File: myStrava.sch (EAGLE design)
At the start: 43 parts, among them Y1 16MHz

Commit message: Avant autoroutage
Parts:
- removed MAX17043: MAX1704X, SparkFun-PowerIC:MAX1704X
- removed R13, R14: 10k, SparkFun-Resistors:RESISTOR1206
- added JTAG1: 2X5_0.05"_CORTEX_DEBUGTH_NOKEY_UNSHROUDED, con-cortex:2X5_0.05"_CORTEX_DEBUGTH_NOKEY_UNSHROUDED
- added U$1: STC3100, STC3100:STC3100
- C1: value 1uF -> 220nF
- C4, C5: value 4.7uF -> 10uF
- R3: value 1k -> 200k/0.1%
- R4: value 180 -> 0.02
- R7: value 4.7k -> 1kOhms
- R8, R9: device SparkFun-Resistors:RESISTOR1206 -> SparkFun-Resistors:RESISTOR0805-RES
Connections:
- removed net N$29: MK20DN512.PTB18, NAV.2
- removed net N$30: MK20DN512.PTB19, NAV.T
- removed net N$31: MK20DN512.PTB0, NAV.1
- removed net N$33: R14.1, SST25.WP
- removed net N$34: R13.2, SST25.HOLD
- new net N$10: N550.NONE1, NAV.2
- new net N$11: N550.SUSPEND, NAV.T
- new net N$12: N550.SLEEP, NAV.1
- new net N$13: N550.NONE2, NAV.C
- new net N$15: MK20DN512.PTB23, SST25.WP
- new net N$24: MK20DN512.PTB22, SST25.HOLD
- new net N$5: C1.1, R7.1, U$1.VIN
- new net N$6: BATT.2, R4.2, U$1.CG
- new net N$9: N550.PORTSEL, SPK.2
- new net VCC: JTAG1.VCC
- net GND: now also C1.2, JTAG1.GND, JTAG1.GND-DETECT, R3.2, R4.1, U$1.GND; no longer BATT.2, C1.1, MAX17043.CTG, MAX17043.GND@4, MAX17043.GND@EP, NAV.C, R7.2, SPK.2
- net MK_SCL: now also U$1.SCL; no longer MAX17043.SCL
- net MK_SDA: now also U$1.SDA; no longer MAX17043.SDA
- net N$3: now also JTAG1.SWDIO/TMS, N550.RST; no longer MK20DN512.PTB1, SPK.1
- net N$4: now also R3.1, U$1.ROSC; no longer C1.2, MAX17043.CELL, R3.2
- net N$7: now also JTAG1.SWDCLK/TCK, N550.NONE3; no longer MAX17043.VDD, R4.2
- net N$8: now also N550.SCLK, SPK.1; no longer MAX17043.QST, R7.1
- net VCC-ISO: now also R7.2, U$1.VCC; no longer R3.1, R4.1
- net VDD: no longer R13.1, R14.2
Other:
- moved on the sheet: C1, NAV, R3, R4, R7, SPK

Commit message: Version avec MK64
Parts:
- added D2: OSRAM, SparkFun-LED:LED-RED1206
- added D3: Diode, adafruit:DIODE_SOD-123FL
- added PTE2, PTE3, RX2, SCL, SDA: MDMK2020T4R7MM, Exposed_pad:MDMK2020T4R7MM
- added R13: 50ohms, SparkFun-Resistors:RESISTOR1206
- added R14: 10K, SparkFun-Resistors:RESISTOR1206
- added TX2: TX2, Exposed_pad:MDMK2020T4R7MM
- renumbered LDO33 to LDO0, U$1 to STC3100
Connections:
- removed net VDD: BMP180.VDD, BMP180.VDDIO, C2.P$1, C3.P$1, C6.P$1, C7.P$1, C8.P$1, C9.P$1, JTAG.VCC, LDO0.OUT, MK20DN512.VBAT, MK20DN512.VDD, MK20DN512.VDD1, MK20DN512.VDD2, MK20DN512.VDD3, MK20DN512.VDD4, MK20DN512.VDD5, MK20DN512.VDDA, MK20DN512.VOUT33, MK20DN512.VREFH, MT3339.VCC, N550.VCC, R12.2, R5.1, R6.1, SD.VCC, SHARP.VDD, SHARP.VDDA, SST25.VDD
- new net END_CHARGE: MCP73831.STAT, MK20DN512.PTB0, R2.2
- new net MK_RX2: MK20DN512.PTE1, RX2.1
- new net MK_TX2: MK20DN512.PTE0, TX2.1
- new net MK_USB_DETECT: MK20DN512.PTE5, R14.1
- new net N$28: MK20DN512.PTE2, PTE2.1
- new net N$30: MK20DN512.PTE3, PTE3.1
- new net N$31: MK20DN512.PTB1, R13.1
- new net USB_V+: C4.1, D1.A, D3.A, MCP73831.VDD, R14.2, USB.VBUS
- net MK_SCL: now also SCL.1
- net MK_SDA: now also SDA.1
- net N$17: now also D2.C, R13.2; no longer MCP73831.STAT, R2.2
- net N$18: now also MK20DN512.PTD1, N550.BR1; no longer C4.1, D1.A, MCP73831.VDD, USB.VBUS
- net N$21: now also MK20DN512.PTD0, N550.SPD_SEL; no longer MK20DN512.PTD4, N550.BR1
- net VCC: now also BMP180.VDD, BMP180.VDDIO, C2.P$1, C3.P$1, C6.P$1, C7.P$1, C8.P$1, C9.P$1, D2.A, JTAG.VCC, LDO0.OUT, MK20DN512.VBAT, MK20DN512.VDD, MK20DN512.VDD1, MK20DN512.VDD2, MK20DN512.VDD3, MK20DN512.VDD4, MK20DN512.VDD5, MK20DN512.VDDA, MK20DN512.VOUT33, MK20DN512.VREFH, MT3339.VCC, N550.VCC, R12.2, R5.1, R6.1, SD.VCC, SHARP.VDD, SHARP.VDDA, SST25.VDD
- net VCC-ISO: now also D3.C
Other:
- moved on the sheet: R8, R9

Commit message: Circuit imprime avec bugs
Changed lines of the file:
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@@
 <instance part="R8" gate="G$1" x="-116.84" y="-129.54"/>
 <instance part="R9" gate="G$1" x="-127" y="-134.62"/>
-<instance part="U$16" gate="G$1" x="-198.12" y="-45.72" rot="R270"/>
+<instance part="U$16" gate="G$1" x="-195.58" y="-45.72" rot="R270"/>
 <instance part="U$11" gate="G$1" x="-218.44" y="-40.64" rot="R90"/>
 <instance part="SUPPLY2" gate="G$1" x="-157.48" y="-40.64" rot="R270"/>
@@
 <pinref part="U$16" gate="G$1" pin="GND"/>
 <pinref part="LDO0" gate="G$1" pin="GND"/>
-<wire x1="-195.58" y1="-45.72" x2="-187.96" y2="-45.72" width="0.1524" layer="91"/>
+<wire x1="-193.04" y1="-45.72" x2="-187.96" y2="-45.72" width="0.1524" layer="91"/>
 </segment>
 <segment>
@@
 <segment>
 <pinref part="SST25" gate="G$1" pin="CE"/>
-<wire x1="129.54" y1="-88.9" x2="96.52" y2="-88.9" width="0.1524" layer="91"/>
-<wire x1="96.52" y1="-88.9" x2="96.52" y2="-121.92" width="0.1524" layer="91"/>
+<wire x1="129.54" y1="-88.9" x2="101.6" y2="-88.9" width="0.1524" layer="91"/>
+<wire x1="101.6" y1="-88.9" x2="101.6" y2="-121.92" width="0.1524" layer="91"/>
 <pinref part="MK20DN512" gate="G$1" pin="PTC0"/>
-<wire x1="96.52" y1="-121.92" x2="45.72" y2="-121.92" width="0.1524" layer="91"/>
-</segment>
-</net>
+<wire x1="101.6" y1="-121.92" x2="45.72" y2="-121.92" width="0.1524" layer="91"/>
+</segment>
+</net>

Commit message: Modif pour le module D52Q
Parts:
- added LDO1: 3.3V/150mA, SparkFun-PowerIC:V_REG_MIC52053.3V
- N550: device ANTAP28:ANTAP28 -> D52Q:ANTAP28
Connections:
- removed net N$13: N550.NONE2, NAV.C
- new net VPERM: LDO1.OUT, MT3339.VBACKUP
- net GND: now also LDO1.GND, NAV.C; no longer N550.GND2
- net MK_RX3: now also N550.P017; no longer N550.TX
- net MK_TX3: now also N550.P016; no longer N550.RX
- net N$10: now also N550.P007, NAV.T; no longer N550.NONE1, NAV.2
- net N$11: now also N550.P006, NAV.2; no longer N550.SUSPEND, NAV.T
- net N$12: now also JTAG1.SWDCLK/TCK, N550.SWDCLK; no longer N550.SLEEP, NAV.1
- net N$18: now also N550.P015; no longer N550.BR1
- net N$2: now also LDO1.EN, LDO1.IN
- net N$21: now also N550.P014; no longer N550.SPD_SEL
- net N$3: now also N550.SWDIO; no longer N550.RST
- net N$7: now also N550.P002, NAV.1; no longer JTAG1.SWDCLK/TCK, N550.NONE3
- net N$8: now also N550.P011; no longer N550.SCLK
- net N$9: now also N550.P008; no longer N550.PORTSEL
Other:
- moved on the sheet: NAV

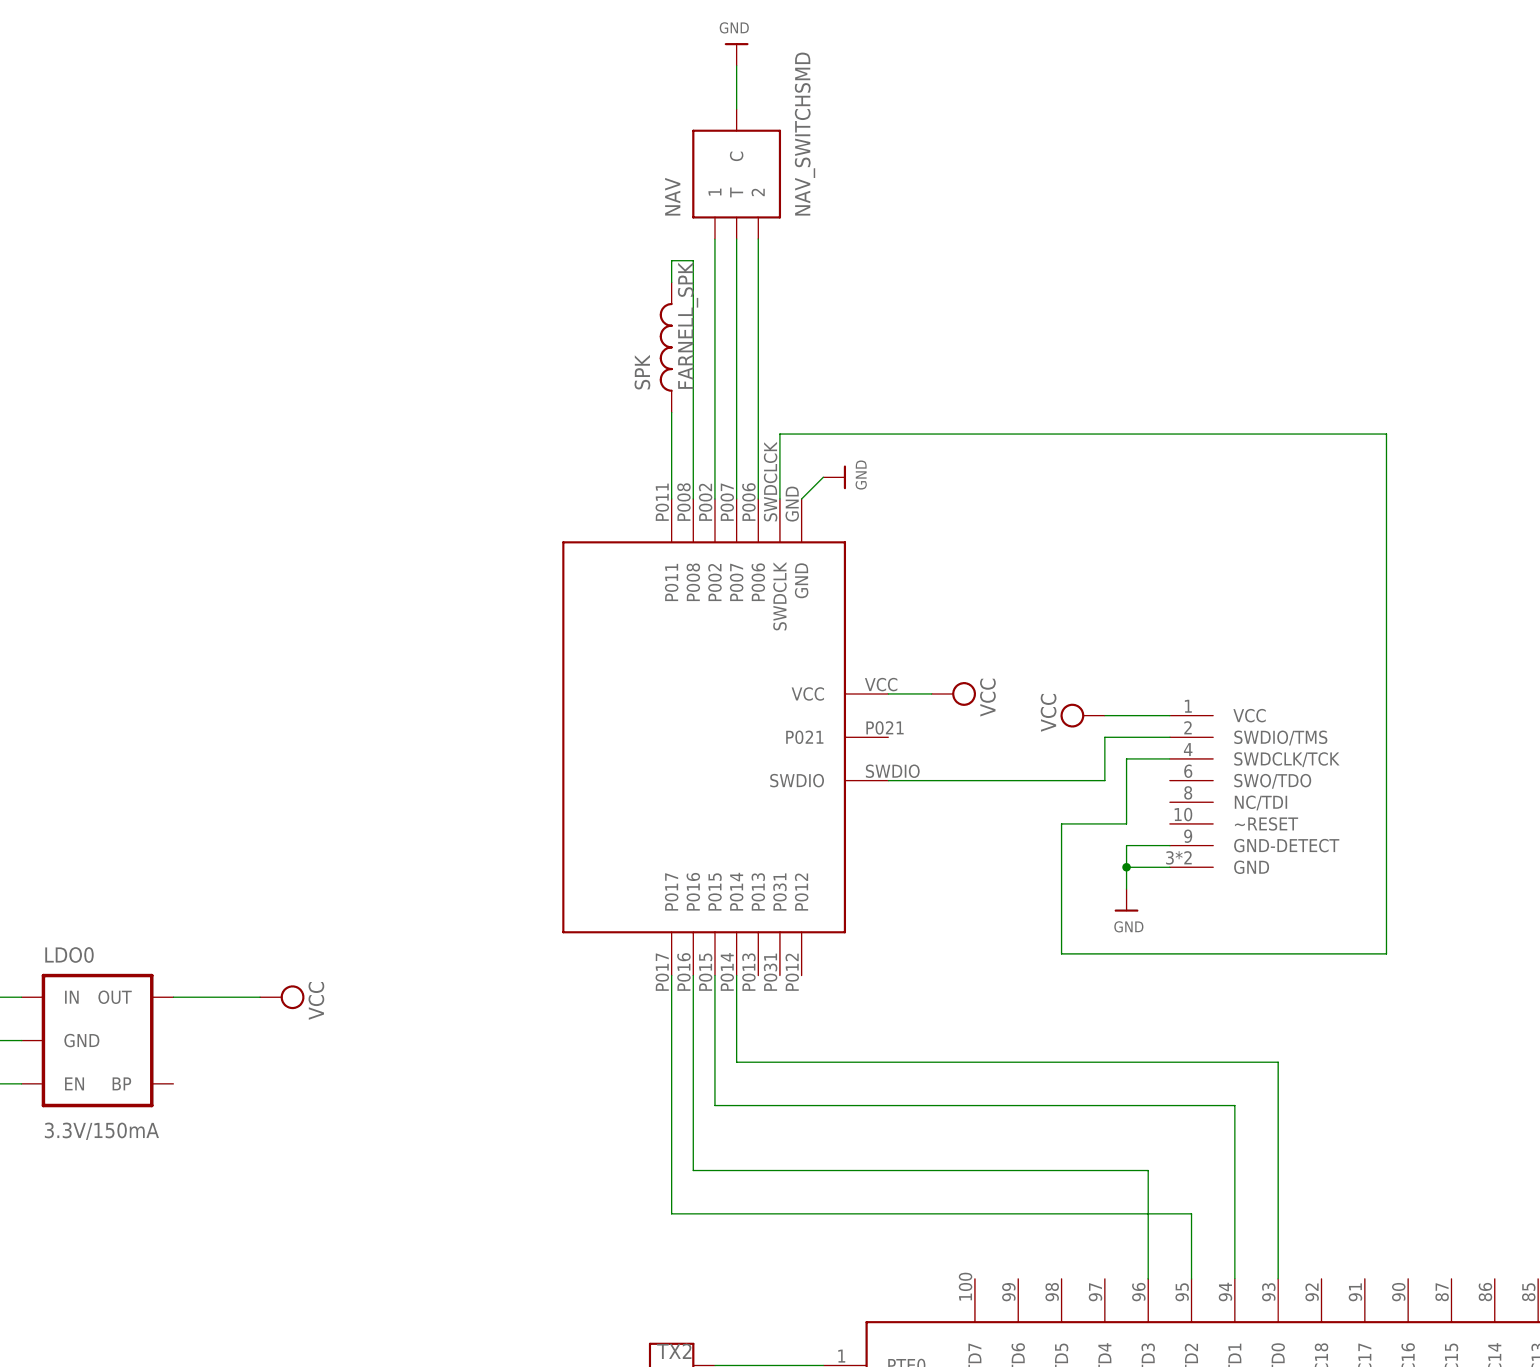
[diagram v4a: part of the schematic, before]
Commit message: Recablage du D52 pour simplifier
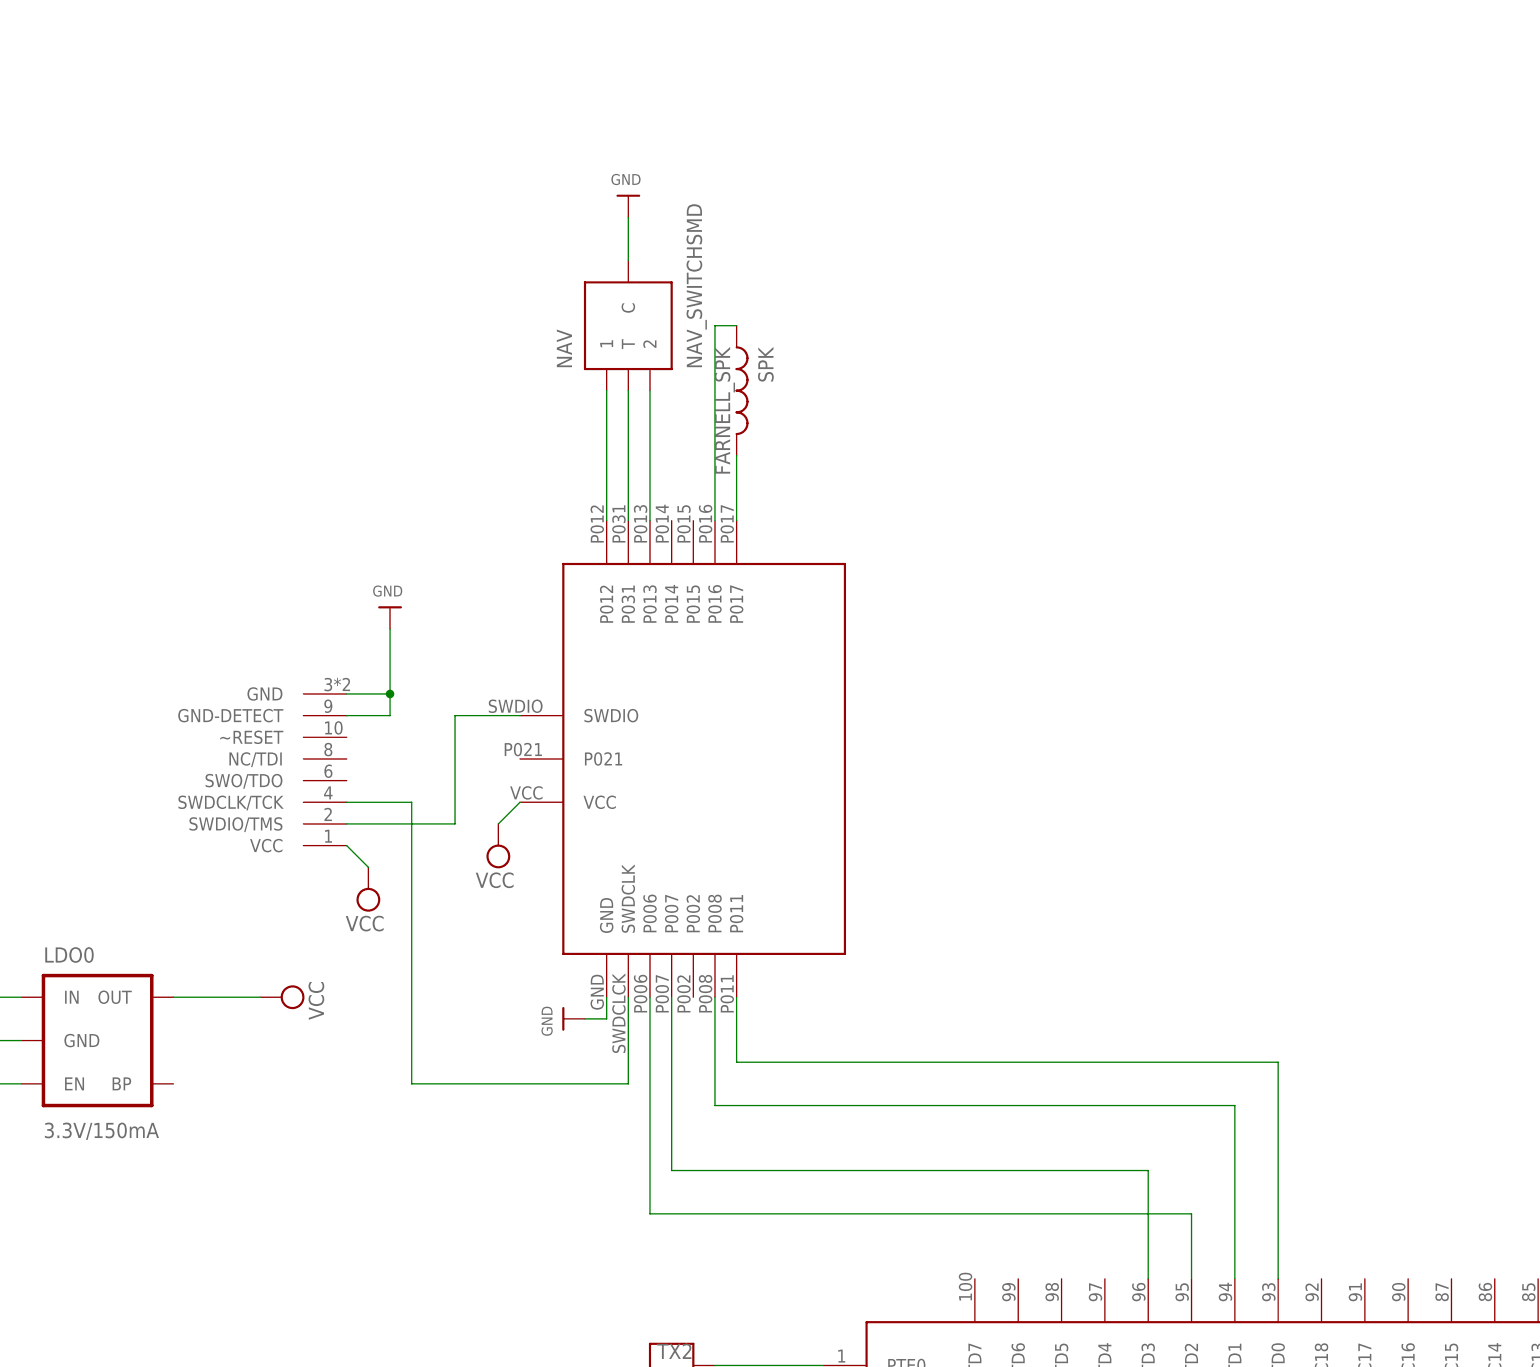
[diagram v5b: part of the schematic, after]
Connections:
- removed net N$11 (its old number): N550.P006, NAV.2
- new net N$3: N550.P017, SPK.2
- net MK_RX3: now also N550.P006; no longer N550.P017
- net MK_TX3: now also N550.P007; no longer N550.P016
- net N$10: now also N550.P013, NAV.2; no longer N550.P007, NAV.T
- net N$18: now also N550.P008; no longer N550.P015
- net N$21: now also N550.P011; no longer N550.P014
- net N$7: now also N550.P016, SPK.1; no longer N550.P002, NAV.1
- net N$8: now also N550.P012, NAV.1; no longer N550.P011, SPK.1
- net N$9: now also N550.P031, NAV.T; no longer N550.P008, SPK.2
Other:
- moved on the sheet: NAV, SPK

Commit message: Envoi a OSH park
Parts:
- removed BMP180: BMP180, SparkFun-Sensors:BMP180
- added MS5637: MS5637, MS5637:MS5637
- MT3333: value GTK -> TITAN2
- renumbered MT3339 to MT3333, N550 to D52Q
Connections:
- net GND: now also MS5637.GND; no longer BMP180.GND
- net MK_SCL: now also MS5637.SCL; no longer BMP180.SCL
- net MK_SDA: now also MS5637.SDA; no longer BMP180.SDA
- net VCC: now also MS5637.VDD; no longer BMP180.VDD, BMP180.VDDIO
